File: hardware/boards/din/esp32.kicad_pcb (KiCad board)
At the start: 4 copper layers, 56.8 x 85 mm, 190 parts, among them J1 PlugIn_Terminal_Screw, J101 USB-C, J102 HR911105A, J103 EXP, J4 5V_IN, Q1 MMBT5401, Q2 MMBT2222A, SW101 TL3342, SW102 TL3342, U1 TLV9351, U101 ESP32-S3-WROOM-1-N8R2, U102 USBLC6-2SC6, U103 AP2114H-3.3TRG1, U104 W5500, U2 LMV321, U3 LMV321, U5 ES8374, U6 LM393, U7 AMS1117-3.3, Y101 25MHz

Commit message: gdoor-din: four JLC Extended parts made fee-free, values kept
Saves $12 of JLC's $3-per-type Extended loading fee (8 charged types -> 4).

- R3/R4 82k: 0402 C2909388 -> 0603 C23254 (Basic).
- R1/R20 130k: 0402 C2909318 -> 0603 C22795 (Preferred Extended).
  The larger pads needed two small reroutes: Net-(J1-Pin_2) between R3
  and R5, and the Net-(C8-Pad2) diagonal next to R20.
- R108 12.4k 1% (C2929935) -> R108 10k (C25744) + new R123 2.4k
  (C25882) in series, node ETH_EXRES_LO; 12.4k exactly. R123 sits below
  R108; the GND via beside R108 pad 2 moved to R123 pad 2.
- Y101 C164045 (CL 20 pF, +-50 ppm) -> C9006 (CL 12 pF, +-20 ppm, Basic),
  same 3225 footprint; C108/C109 33 pF -> 15 pF (C1548). eth_sim.py puts
  the pull at -5.5..+18.5 ppm, worst case ~+48.5 ppm with tolerance and
  temperature, inside 802.3u's +-50 ppm.

DRC (zone refill): 0 errors, 0 unconnected, schematic parity clean.
Production files regenerated with jlcfab.py. mcu_eth.kicad_sch was
rewritten in compact s-expression layout by the Konnect schematic tool;
a netlist comparison shows only the changes above.

Also contains an unrelated one-line change from another session: J101's
3D-model offset (y 0.294 -> -1.045) in esp32.kicad_pcb.

Co-Authored-By: Claude Opus 5.5 <noreply@anthropic.com>
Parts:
- added R123: 2.4k 1%, Resistor_SMD:R_0402_1005Metric, F.Cu at (104.1, 102.2)
- C108, C109: value 33p -> 15p
- R1, R20, R3, R4: footprint Library:R_0402_1005Metric_Pad0.72x0.64mm_HandSolder -> Resistor_SMD:R_0603_1608Metric
- R108: value 12.4k 1% -> 10k 1%
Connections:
- R108 pad 2: GND -> /MCU, USB, Power, Ethernet/ETH_EXRES_LO
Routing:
- net /MCU, USB, Power, Ethernet/ETH_EXRES_LO: track 0.00 -> 0.94 mm
- net Net-(J1-Pin_2): track 12.3 -> 12.9 mm

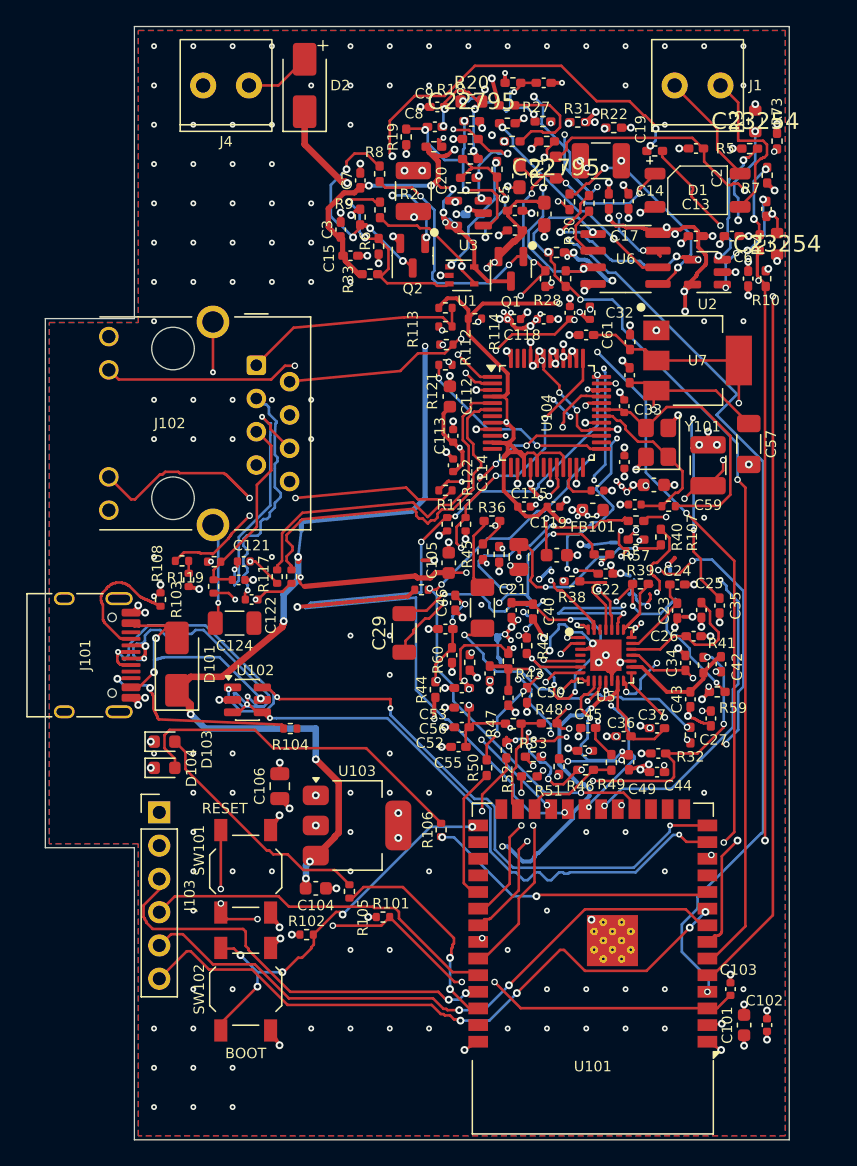
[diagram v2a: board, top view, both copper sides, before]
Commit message: gdoor-din: every part gets a 0.5 mm designator, J4 fitted
Designators shrink from 0.8/0.12 to 0.5/0.1 mm and all 190 are shown,
each placed next to its part clear of pads, other silkscreen and the
other parts' bodies. The DRU and project text-height minimums follow.
The MPN fields that printed on R1, R3, R4 and R20 are hidden.

The screw terminals get labels: J4 "-", "+" and "5V" under its pins,
J1 "~" on both sides and "BUS" (the MB10S bridge makes it polarity-free).

J4 is no longer DNP or excluded from the BOM, in schematic and board.
It joins J1 in jlcfab.py's HAND_SOLDERED, so the JLC BOM and CPL are
unchanged.

Co-Authored-By: Claude Opus 5.5 <noreply@anthropic.com>
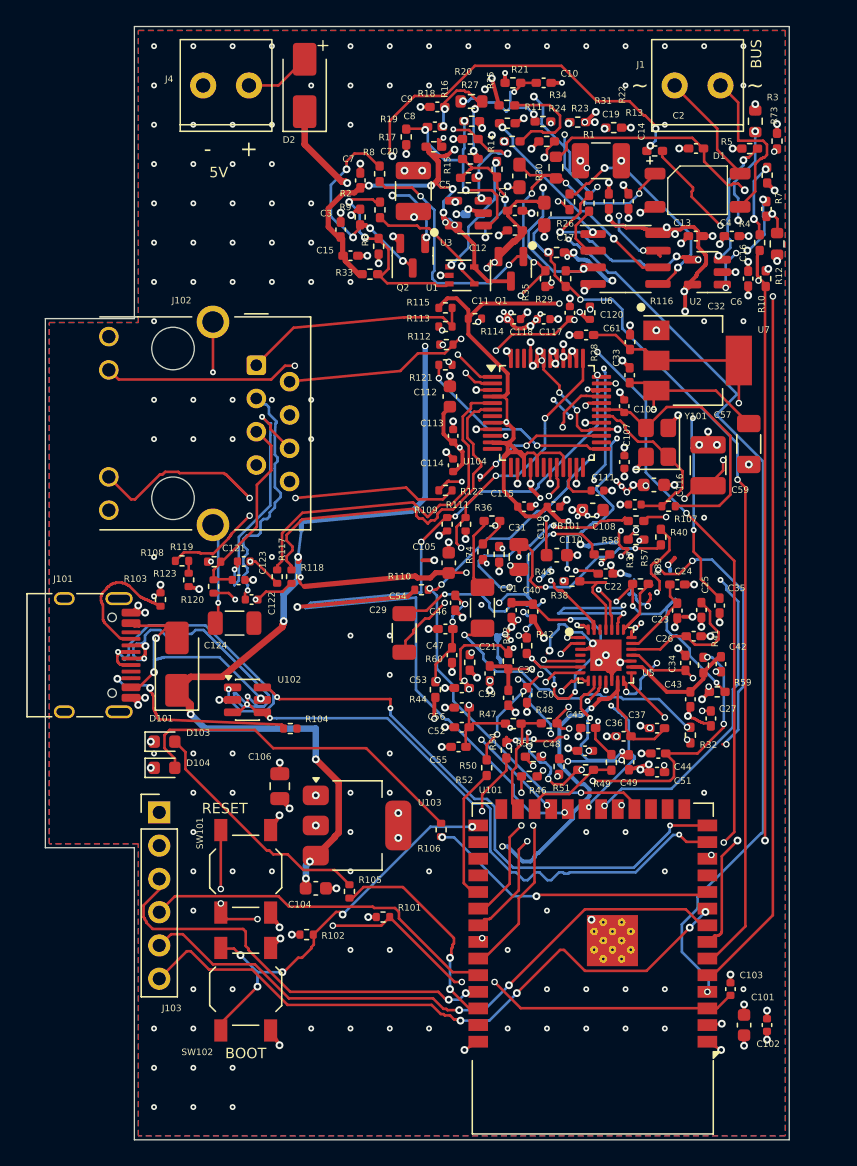
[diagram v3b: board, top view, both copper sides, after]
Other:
- board text added: "+"
- board text added: "-"
- board text added: "5V"
- board text added: "BUS"
- board text added: "~"
